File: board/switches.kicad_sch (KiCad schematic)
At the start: 3 parts, among them Q1 BUK7880-55A, U1 LTC7001

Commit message: Changed Flags
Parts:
- renumbered 0.1u to 0.1u1
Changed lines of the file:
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@@
 		(on_board yes)
 		(dnp no)
-		(property "Reference" "0.1u"
+		(property "Reference" "0.1u1"
 			(at 140.97 77.47 0)
 			(effects
@@
 			(project ""
 				(path "/7eaa639d-7062-45e7-be05-1c2855431307/d051b168-830a-4a55-b5cd-142fa18015a1"
-					(reference "0.1u")
+					(reference "0.1u1")
 					(unit 1)
 				)

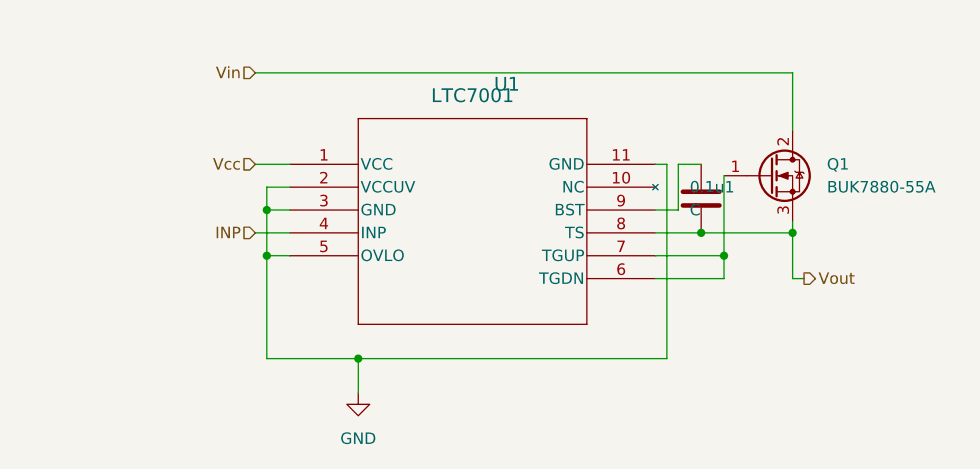
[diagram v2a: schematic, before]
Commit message: switch the LTC7001 gate driver with the LT1910
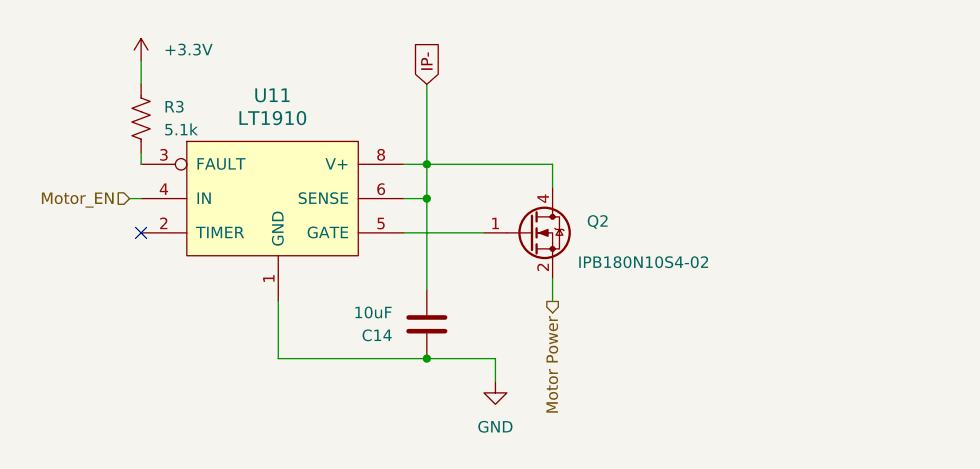
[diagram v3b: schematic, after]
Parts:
- removed 0.1u1: C, symbol Device:C
- removed Q1: BUK7880-55A, Package_TO_SOT_SMD:SOT-223-3_TabPin2, symbol Transistor_FET:BUK7880-55A
- removed U1: LTC7001, 05-08-1664_ADI, symbol LTC7001:LTC7001EMSE-PBF
- added C14: 10uF, Capacitor_SMD:C_1206_3216Metric_Pad1.33x1.80mm_HandSolder, symbol Device:C
- added Q2: IPB180N10S4-02, Package_TO_SOT_SMD:TO-263-6, symbol Transistor_FET:IPB180N10S4-02
- added R3: 5.1k, symbol Device:R_US
- added U11: LT1910, Package_SO:SOIC-8_3.9x4.9mm_P1.27mm, symbol MRDT_ICs:LT1910
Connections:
- net GND: now also C14.1, U11.1 (GND)
- new net: Q2.1 (G), U11.5 (GATE)
- new net: R3.2, U11.3 (FAULT)
- new net +3.3V: R3.1
- new net IP-: C14.2, Q2.4 (D), U11.6 (SENSE), U11.8 (V+)
- new net Motor Power: Q2.2 (S), Q2.3 (S), Q2.5 (S), Q2.6 (S), Q2.7 (S)
- new net Motor_EN: U11.4 (IN)
- no-connect marks 0 -> 1

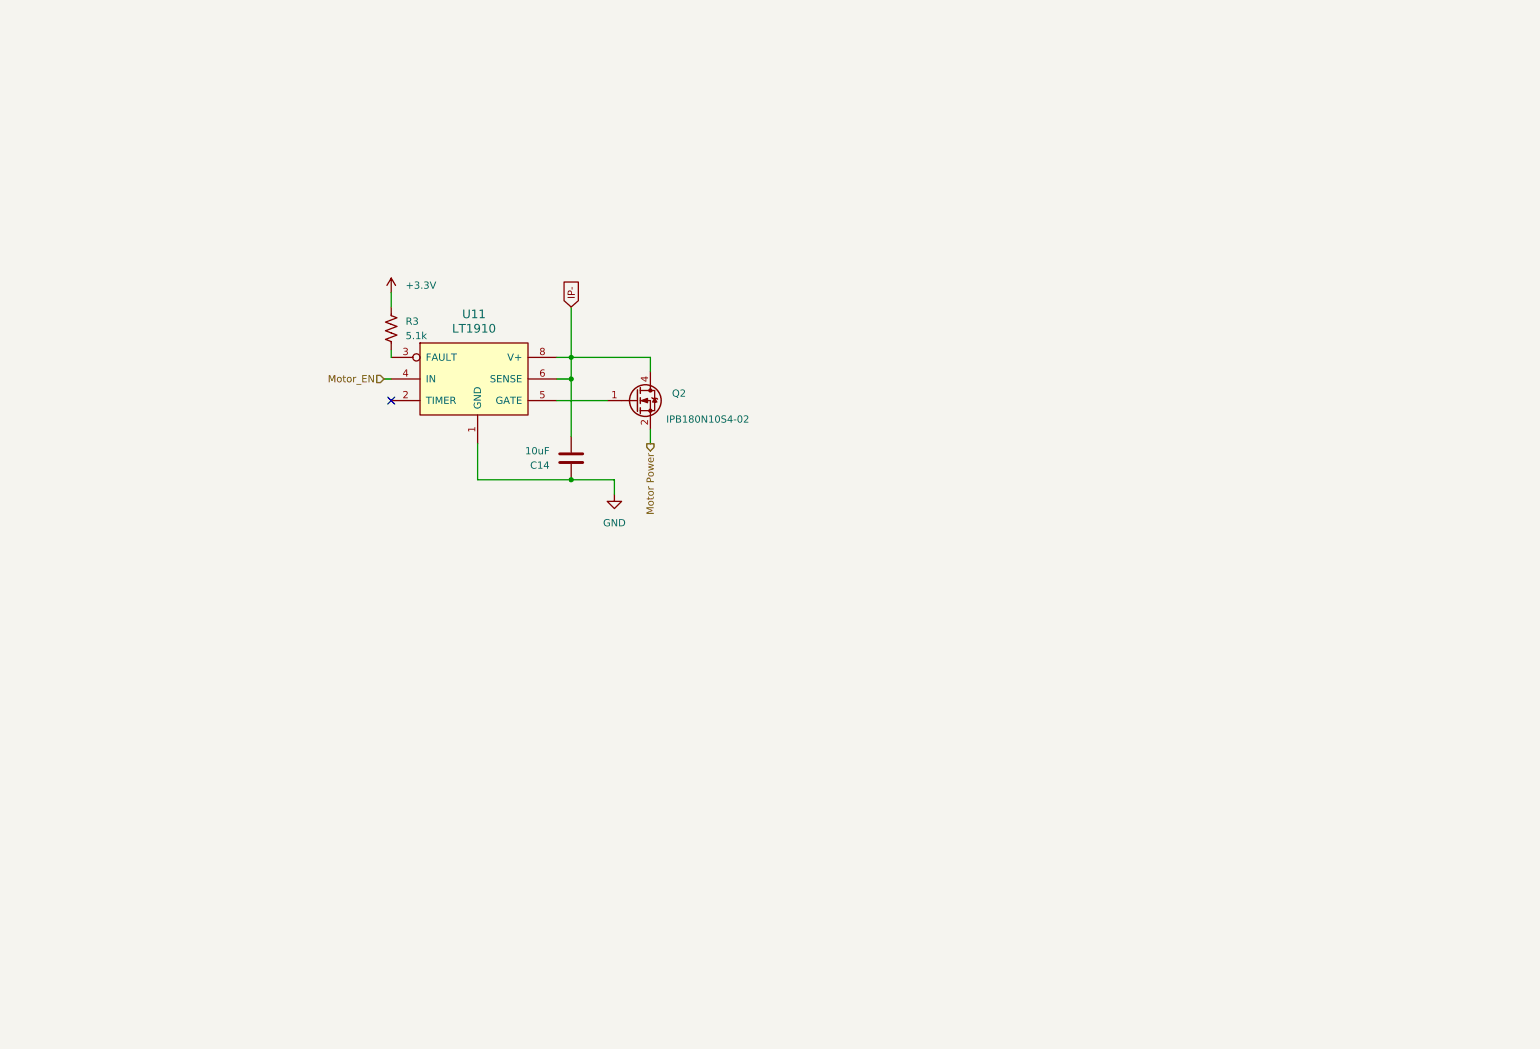
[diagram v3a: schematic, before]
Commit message: create 5 switching circuits
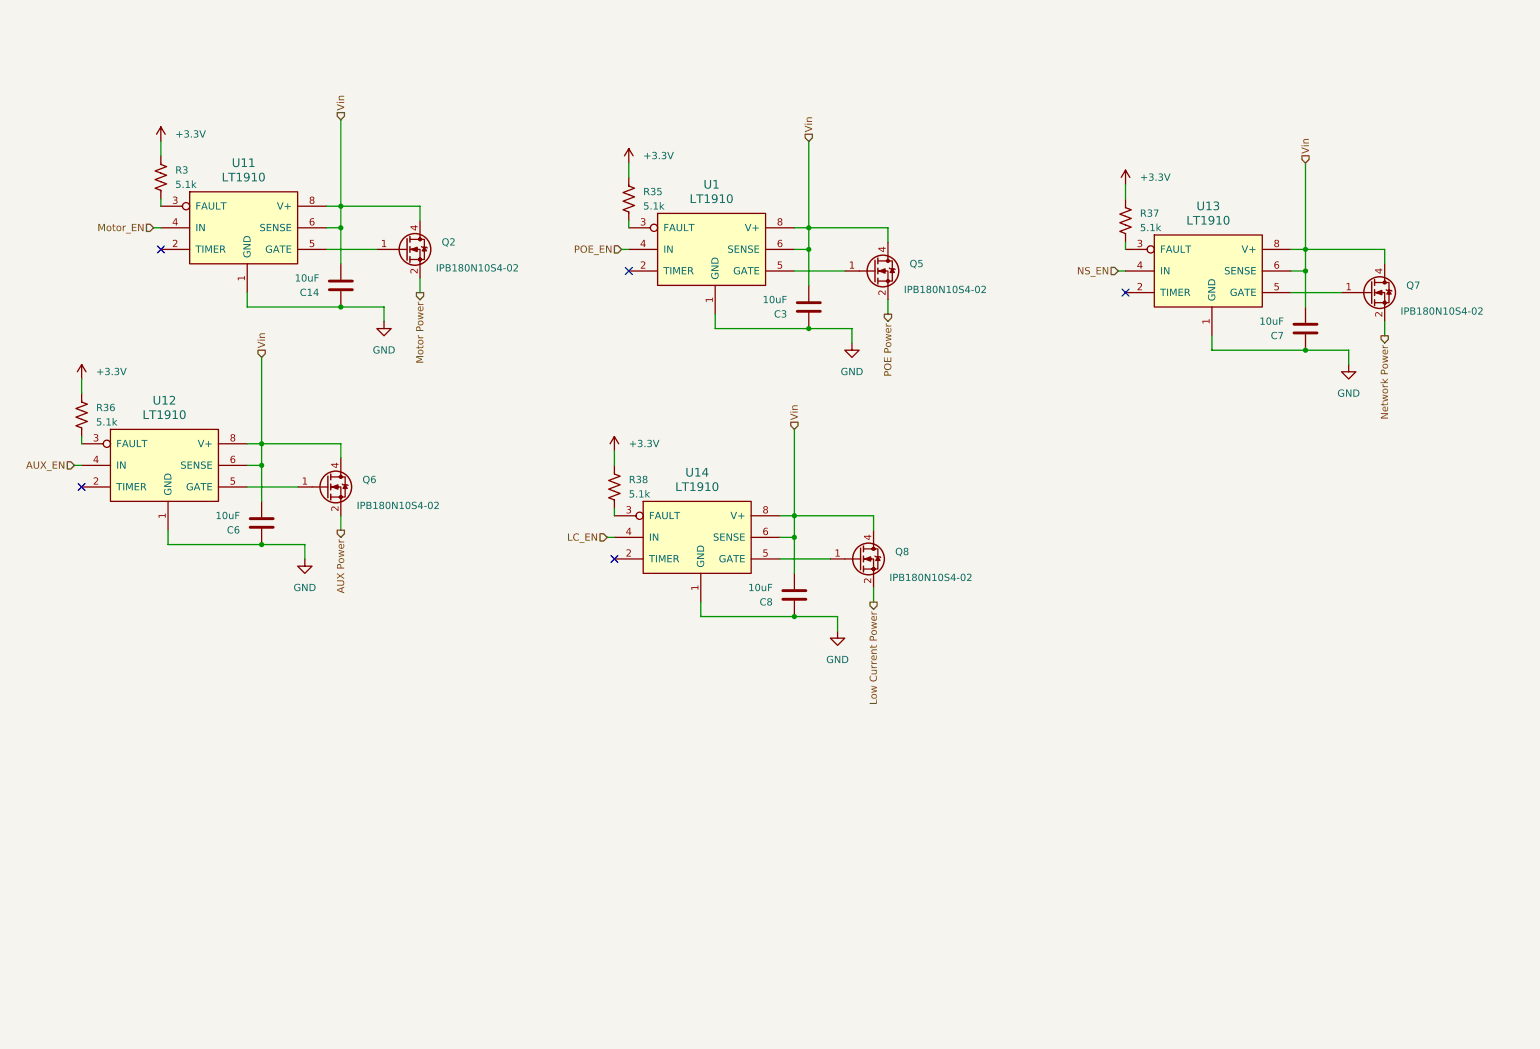
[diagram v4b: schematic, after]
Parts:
- added C3, C6, C7, C8: 10uF, Capacitor_SMD:C_1206_3216Metric_Pad1.33x1.80mm_HandSolder, symbol Device:C
- added Q5, Q6, Q7, Q8: IPB180N10S4-02, Package_TO_SOT_SMD:TO-263-6, symbol Transistor_FET:IPB180N10S4-02
- added R35, R36, R37, R38: 5.1k, symbol Device:R_US
- added U1, U12, U13, U14: LT1910, Package_SO:SOIC-8_3.9x4.9mm_P1.27mm, symbol MRDT_ICs:LT1910
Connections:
- net +3.3V: now also R35.1, R36.1, R37.1, R38.1
- net GND: now also C3.1, C6.1, C7.1, C8.1, U1.1 (GND), U12.1 (GND), U13.1 (GND), U14.1 (GND)
- net IP- renamed Vin
- net Vin: now also C3.2, C6.2, C7.2, C8.2, Q5.4 (D), Q6.4 (D), Q7.4 (D), Q8.4 (D), U1.6 (SENSE), U1.8 (V+), U12.6 (SENSE), U12.8 (V+), U13.6 (SENSE), U13.8 (V+), U14.6 (SENSE), U14.8 (V+)
- new net: Q7.1 (G), U13.5 (GATE)
- new net: R38.2, U14.3 (FAULT)
- new net: Q8.1 (G), U14.5 (GATE)
- new net: R37.2, U13.3 (FAULT)
- new net: R35.2, U1.3 (FAULT)
- new net: Q6.1 (G), U12.5 (GATE)
- new net: Q5.1 (G), U1.5 (GATE)
- new net: R36.2, U12.3 (FAULT)
- new net AUX Power: Q6.2 (S), Q6.3 (S), Q6.5 (S), Q6.6 (S), Q6.7 (S)
- new net AUX_EN: U12.4 (IN)
- new net LC_EN: U14.4 (IN)
- new net Low Current Power: Q8.2 (S), Q8.3 (S), Q8.5 (S), Q8.6 (S), Q8.7 (S)
- new net NS_EN: U13.4 (IN)
- new net Network Power: Q7.2 (S), Q7.3 (S), Q7.5 (S), Q7.6 (S), Q7.7 (S)
- new net POE Power: Q5.2 (S), Q5.3 (S), Q5.5 (S), Q5.6 (S), Q5.7 (S)
- new net POE_EN: U1.4 (IN)
- no-connect marks 1 -> 5
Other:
- moved on the sheet: C14, Q2, R3, U11

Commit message: add labels to switching circuits
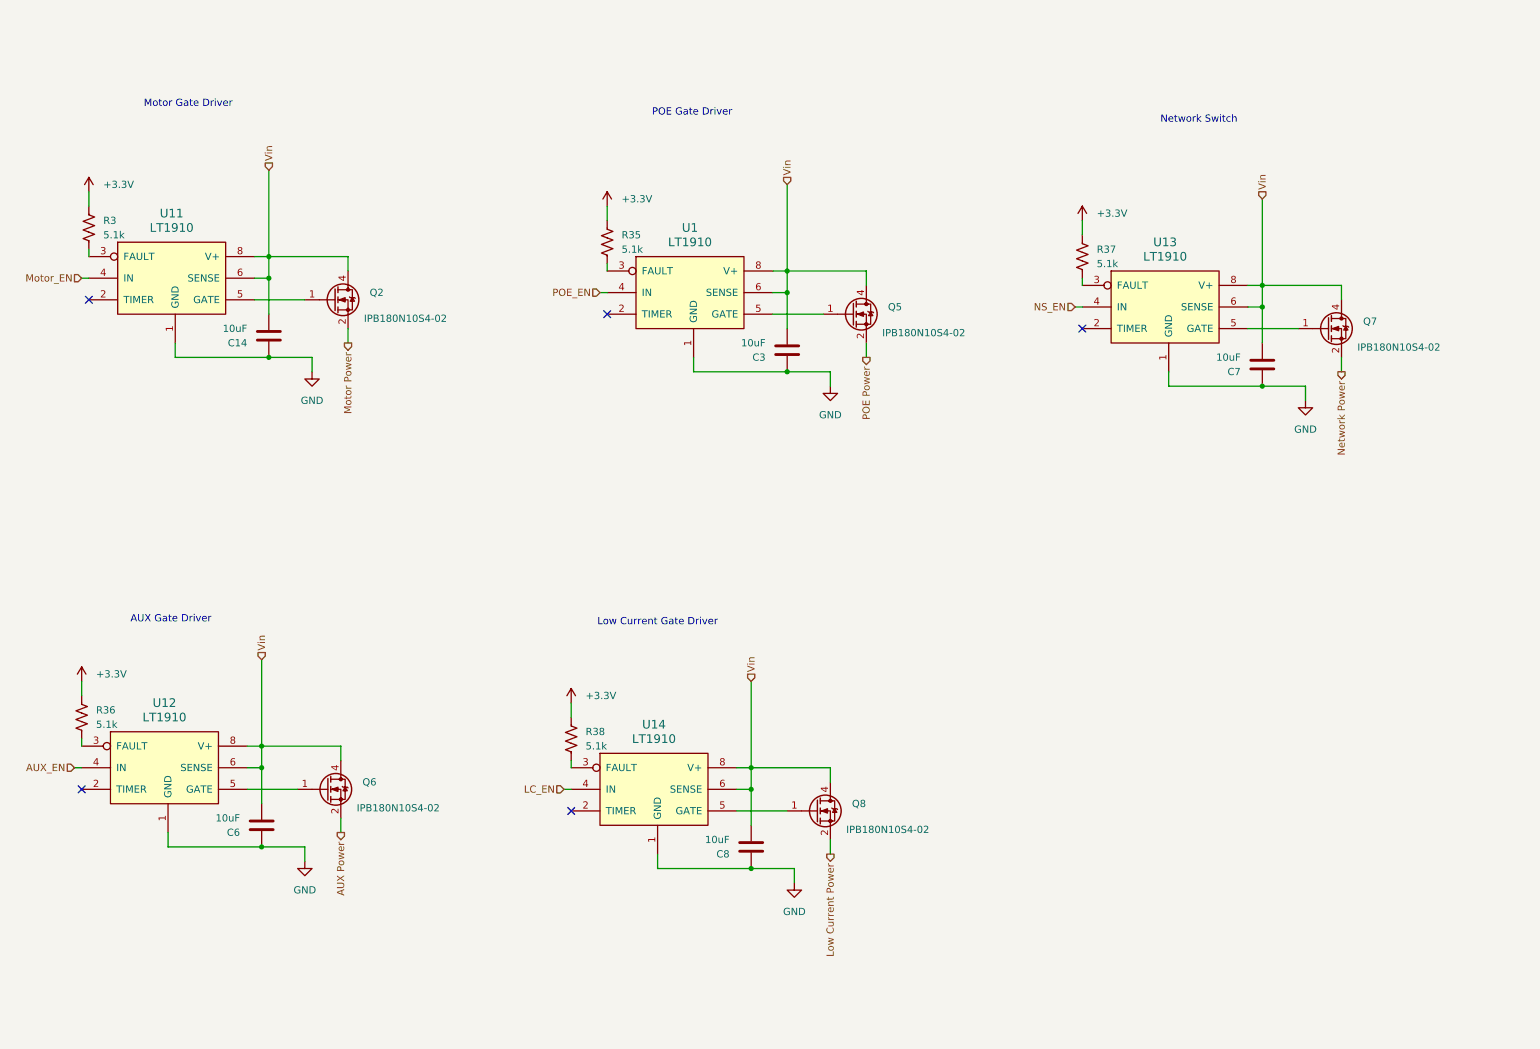
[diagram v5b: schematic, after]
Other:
- note added: "AUX Gate Driver"
- note added: "Low Current Gate Driver"
- note added: "Motor Gate Driver"
- note added: "Network Switch"
- note added: "POE Gate Driver"
- moved on the sheet: C14, C3, C6, C7, C8, Q2, Q5, Q6, Q7, Q8, R3, R35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

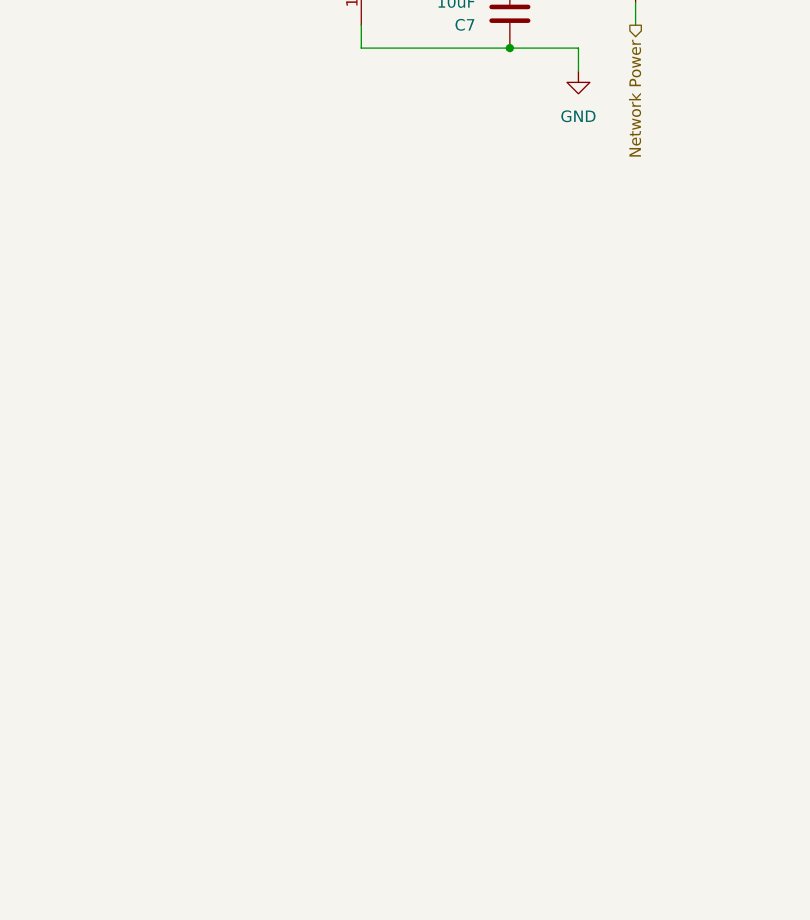
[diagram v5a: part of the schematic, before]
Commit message: add POE
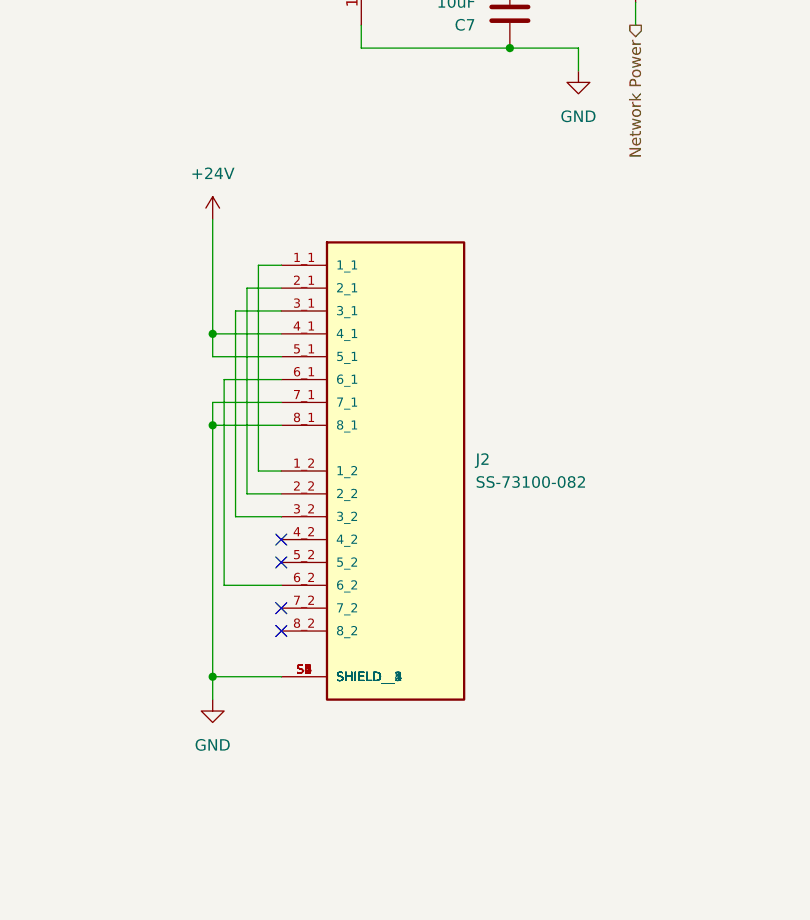
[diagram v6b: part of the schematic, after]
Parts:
- added J2: SS-73100-082, SS-73100-082:BEL_SS-73100-082, symbol PowerManagementBoard:SS-73100-082
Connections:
- net GND: now also J2.7_1, J2.8_1, J2.S1 (SHIELD), J2.S2 (SHIELD__1), J2.S3 (SHIELD__2), J2.S4 (SHIELD__3), J2.S5 (SHIELD__4), J2.S6 (SHIELD__5)
- new net: J2.1_1, J2.1_2
- new net: J2.2_1, J2.2_2
- new net: J2.3_1, J2.3_2
- new net: J2.6_1, J2.6_2
- new net +24V: J2.4_1, J2.5_1
- no-connect marks 5 -> 9
